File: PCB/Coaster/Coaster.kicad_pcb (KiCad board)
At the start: 2 copper layers, 202 x 100 mm, 88 parts, among them J1 Join, J2 Shelly, J3 USB-C, P1 TestPoint, P10 TestPoint, P11 TestPoint, P12 TestPoint, P13 TestPoint, P14 TestPoint, P15 TestPoint, P16 TestPoint, P17 TestPoint, P2 TestPoint, P3 TestPoint, P4 TestPoint, P5 TestPoint, P6 TestPoint, P7 TestPoint, P8 TestPoint, P9 TestPoint, T1 TestPoint, T10 TestPoint, T11 TestPoint, T12 TestPoint, T13 TestPoint, T14 TestPoint, T15 TestPoint, T16 TestPoint, T17 TestPoint, T2 TestPoint, T3 TestPoint, T4 TestPoint, T5 TestPoint, T6 TestPoint, T7 TestPoint, T8 TestPoint, T9 TestPoint, U1 ESP32-PICO-MINI-02, U2 LMR16006XDDCR, U3 QR

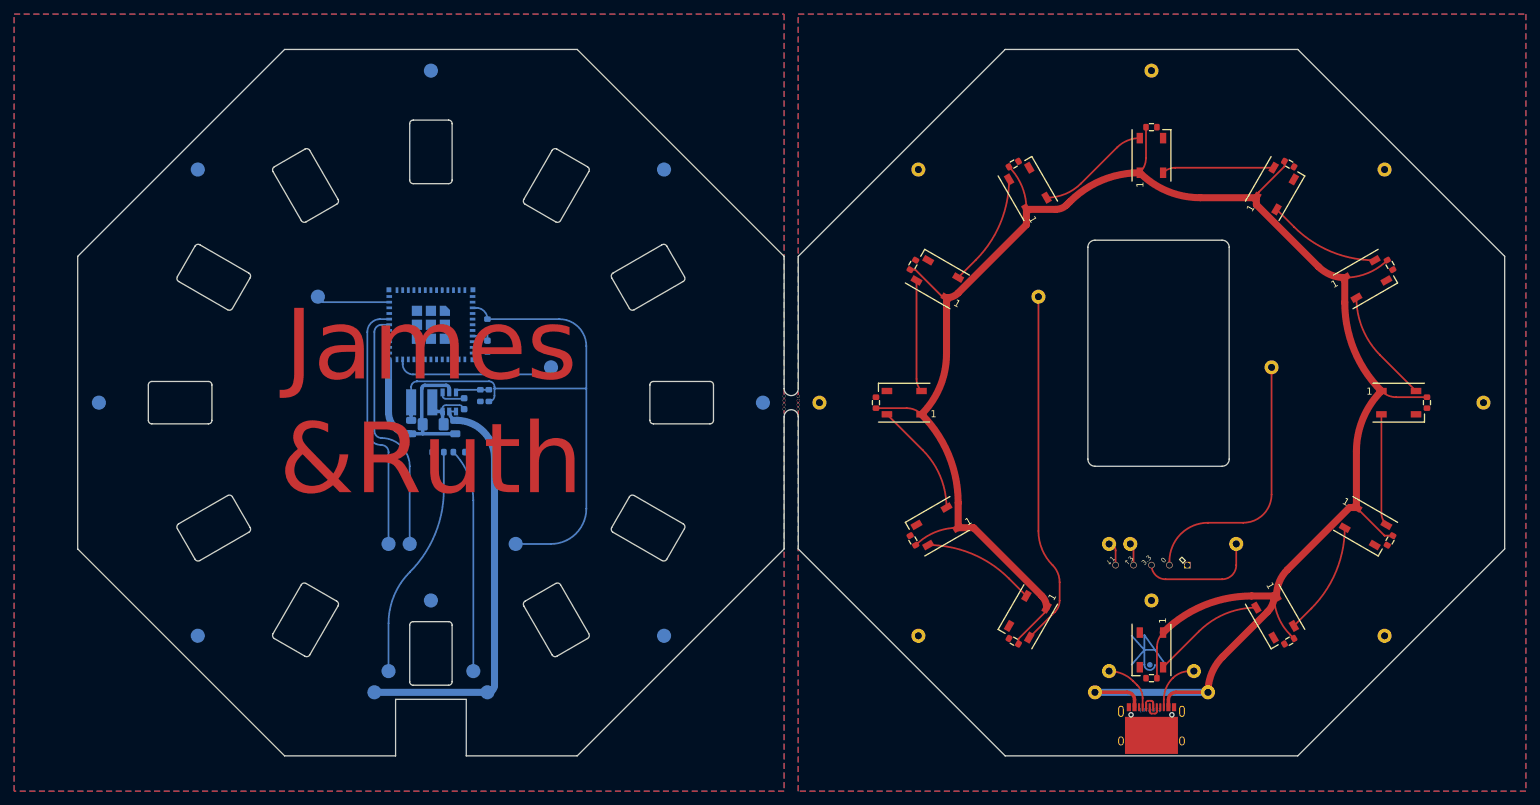
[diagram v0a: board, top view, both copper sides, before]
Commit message: Reworked for rubber feet
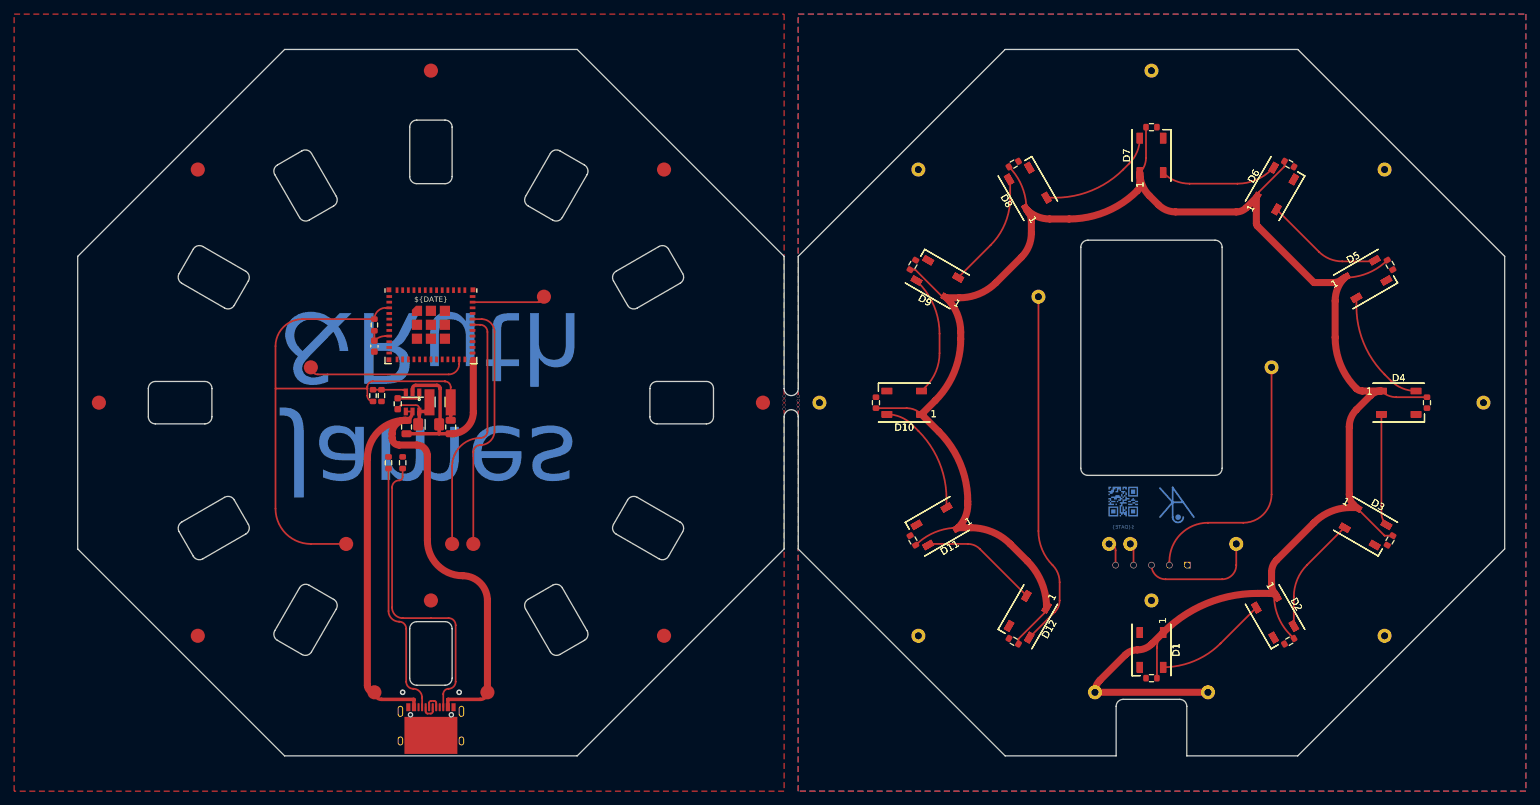
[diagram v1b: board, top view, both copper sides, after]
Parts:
- removed P3, P4: TestPoint, RevK:PAD
- removed T3, T4: TestPoint, RevK:PAD-LINK
- added D1: WS2818B, RevK:SMD5050, F.Cu at (201.0, 135.0)
- added D10: WS2818B, RevK:SMD5050, F.Cu at (166.0, 100.0)
- added D11: WS2818B, RevK:SMD5050, F.Cu at (170.7, 117.5)
- added D12: WS2818B, RevK:SMD5050, F.Cu at (183.5, 130.3)
- added D2: WS2818B, RevK:SMD5050, F.Cu at (218.5, 130.3)
- added D3: WS2818B, RevK:SMD5050, F.Cu at (231.3, 117.5)
- added D4: WS2818B, RevK:SMD5050, F.Cu at (236.0, 100.0)
- added D5: WS2818B, RevK:SMD5050, F.Cu at (231.3, 82.5)
- added D6: WS2818B, RevK:SMD5050, F.Cu at (218.5, 69.7)
- added D7: WS2818B, RevK:SMD5050, F.Cu at (201.0, 65.0)
- added D8: WS2818B, RevK:SMD5050, F.Cu at (183.5, 69.7)
- added D9: WS2818B, RevK:SMD5050, F.Cu at (170.7, 82.5)
- C13, C14, C15, C16, D14, L1, P1, P10, P11, P12, P13, P14, P15, P16, P17, P2, P5, P6, P7, P8, P9, R1, R5, R6, R7, R8, U1, U2: moved to F.Cu
- D1, D10, D11, D12, D2, D3, D4, D5, D6, D7, D8, D9: value WS2812B -> WS2818B; footprint LED_SMD:LED_WS2812B_PLCC4_5.0x5.0mm_P3.2mm -> RevK:SMD5050
- J2: moved to B.Cu
- moved J3 102.0 mm to (99.0, 145.6)
- moved P5 94.0 mm to (52.0, 100.0), turned to 0 degrees
- moved P6 94.0 mm to (146.0, 100.0), turned to 0 degrees
- moved P14 66.0 mm to (132.0, 133.0), turned to 0 degrees
- moved P15 66.0 mm to (66.0, 133.0), turned to 0 degrees
- moved P16 66.0 mm to (66.0, 67.0), turned to 0 degrees
- moved P17 66.0 mm to (132.0, 67.0), turned to 0 degrees
- moved P12 34.0 mm to (82.0, 95.0), turned to 0 degrees
- moved U3 33.3 mm to (197.0, 114.0), turned to 180 degrees
- moved P13 32.0 mm to (115.0, 85.0), turned to 0 degrees
- moved P11 24.0 mm to (87.0, 120.0), turned to 0 degrees
- moved Logo1 21.3 mm to (204.0, 114.1)
- moved R7 16.4 mm to (90.8, 99.0)
- moved C16 16.0 mm to (91.0, 92.0)
- moved P1 16.0 mm to (107.0, 141.0), turned to 0 degrees
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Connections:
- J3 pad A1: GND2 -> GND
- J3 pad A12: GND2 -> GND
- J3 pad A4: VCC -> VBUS
- J3 pad A9: VCC -> VBUS
- J3 pad B1: GND2 -> GND
- J3 pad B12: GND2 -> GND
- J3 pad B4: VCC -> VBUS
- J3 pad B9: VCC -> VBUS
- J3 pad S1: GND2 -> GND
- R5 pad 1: Net-(P3-Pad1) -> Net-(J3-PadB5)
- R6 pad 2: Net-(P4-Pad1) -> Net-(J3-PadA5)
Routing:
- net VBUS: track 58.8 -> 105.3 mm
- net Net-(J3-PadB5): track 7.09 -> 43.3 mm
- net Net-(P3-Pad1): track 33.0 -> 0.00 mm
- net Net-(P4-Pad1): track 31.7 -> 0.00 mm
- net Net-(J3-PadA5): track 7.90 -> 36.3 mm
- net VCC: track 319.7 -> 321.5 mm
- net Net-(D10-Pad2): track 15.8 -> 17.2 mm
- net Net-(D10-Pad4): track 16.1 -> 17.0 mm
- net Net-(D7-Pad4): track 16.1 -> 17.0 mm
- net Net-(D4-Pad4): track 16.1 -> 17.0 mm
- net Net-(D6-Pad4): track 15.8 -> 16.6 mm
- net Net-(D11-Pad4): track 16.1 -> 16.9 mm
- net Net-(D5-Pad4): track 16.1 -> 16.8 mm
- net Net-(D2-Pad4): track 16.1 -> 16.6 mm
- net GND: vias 0 -> 2
- removed copper zone on B.Cu, net GND
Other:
- outline, holes or cut-outs redrawn
- board text added: "LED GPIO 22"

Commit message: Tidy
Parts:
- moved Logo1 1.00 mm to (205.0, 114.1)
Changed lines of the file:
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@@
   )
   (footprint "RevK:AJK" (layer "B.Cu")
-    (at 204 114.1 180)
+    (at 205 114.1 180)
     (property "Note" "Non part, PCB printed")
     (property "Sheetfile" "Coaster.kicad_sch")

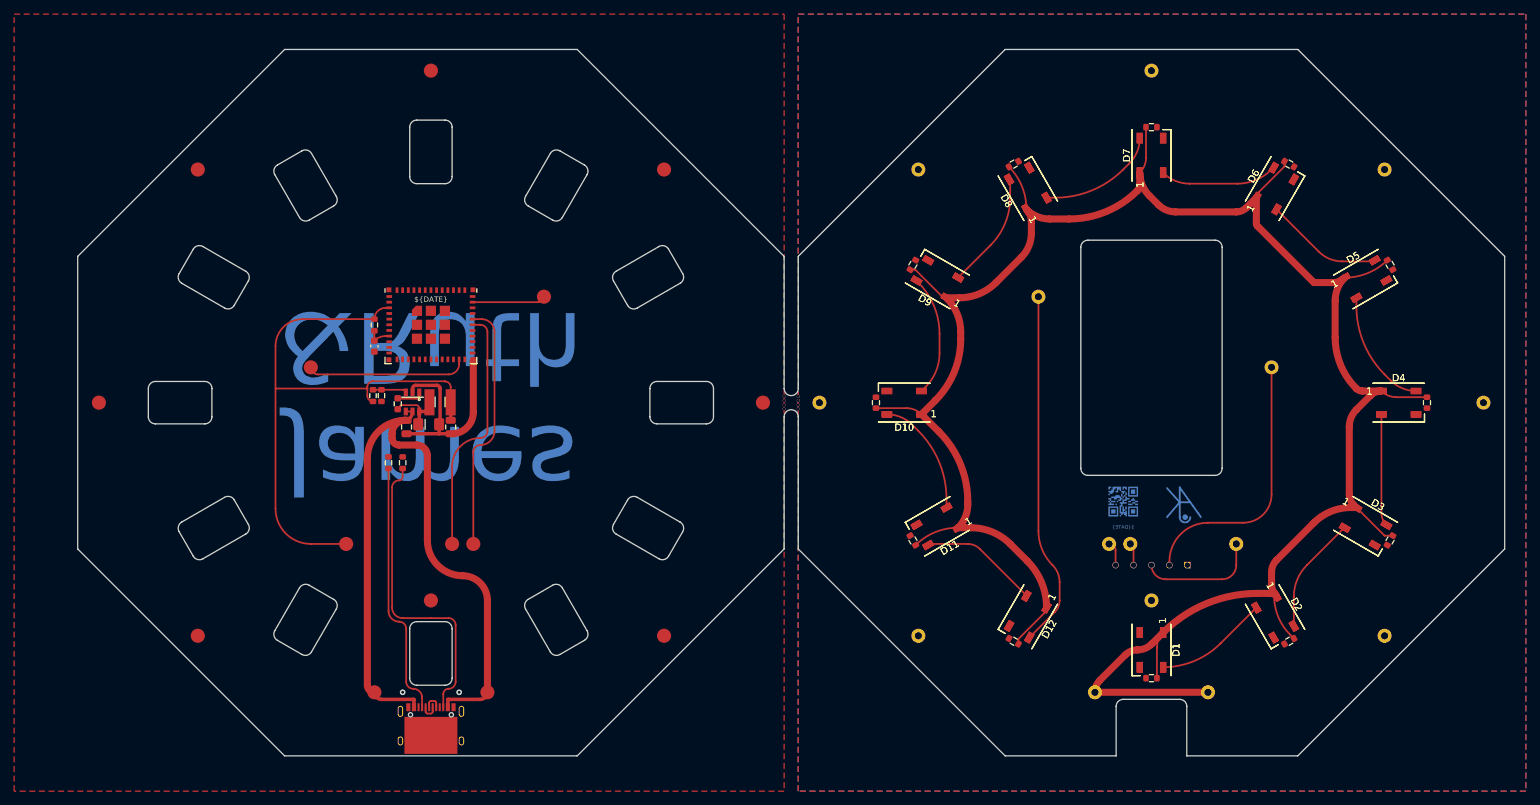
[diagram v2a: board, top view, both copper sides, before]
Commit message: 12 sided
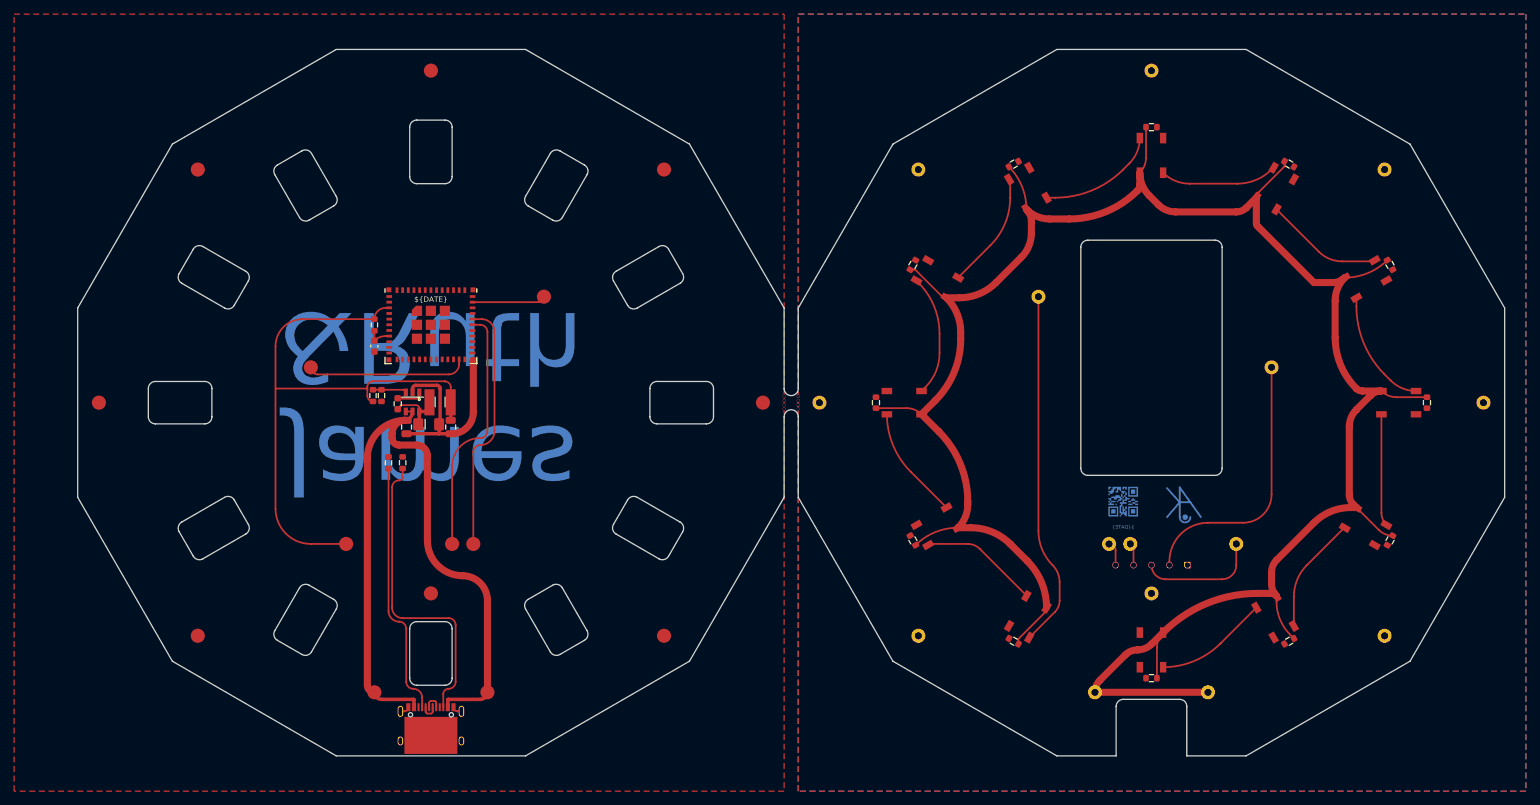
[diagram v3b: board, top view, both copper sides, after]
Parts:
- removed the D1 at (201.0, 135.0) (x2)
- removed the D10 at (166.0, 100.0) (x2)
- removed the D11 at (170.7, 117.5) (x2)
- removed the D12 at (183.5, 130.3) (x2)
- removed the D2 at (218.5, 130.3) (x2)
- removed the D3 at (231.3, 117.5) (x2)
- removed the D4 at (236.0, 100.0) (x2)
- removed the D5 at (231.3, 82.5) (x2)
- removed the D6 at (218.5, 69.7) (x2)
- removed the D7 at (201.0, 65.0) (x2)
- removed the D8 at (183.5, 69.7) (x2)
- removed the D9 at (170.7, 82.5) (x2)
- added D1: WS2818B, RevK:SMD5050, F.Cu at (201.0, 135.0)
- added D10: WS2818B, RevK:SMD5050, F.Cu at (166.0, 100.0)
- added D11: WS2818B, RevK:SMD5050, F.Cu at (170.7, 117.5)
- added D12: WS2818B, RevK:SMD5050, F.Cu at (183.5, 130.3)
- added D2: WS2818B, RevK:SMD5050, F.Cu at (218.5, 130.3)
- added D3: WS2818B, RevK:SMD5050, F.Cu at (231.3, 117.5)
- added D4: WS2818B, RevK:SMD5050, F.Cu at (236.0, 100.0)
- added D5: WS2818B, RevK:SMD5050, F.Cu at (231.3, 82.5)
- added D6: WS2818B, RevK:SMD5050, F.Cu at (218.5, 69.7)
- added D7: WS2818B, RevK:SMD5050, F.Cu at (201.0, 65.0)
- added D8: WS2818B, RevK:SMD5050, F.Cu at (183.5, 69.7)
- added D9: WS2818B, RevK:SMD5050, F.Cu at (170.7, 82.5)
- moved P8 1.00 mm to (99.0, 127.0)
- moved T8 1.00 mm to (201.0, 127.0)
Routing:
- net GND: track 12.0 -> 14.9 mm, vias 2 -> 0
- net Net-(D10-Pad4): track 17.0 -> 16.1 mm
- net Net-(D11-Pad4): track 16.9 -> 16.4 mm
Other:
- outline, holes or cut-outs redrawn

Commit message: Much tidying
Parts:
- removed P13, P14, P15, P16, P17: TestPoint, RevK:PAD
- removed R6: 5K1, RevK:R_0603
- removed R7: 100k 1%, RevK:R_0603
- removed R8: 30k 1%, RevK:R_0603
- removed T13, T14, T15, T16, T17: TestPoint, RevK:PAD-LINK
- added C17: 10nF, RevK:C_0603, F.Cu at (229.3, 80.9)
- added C18: 10nF, RevK:C_0603, F.Cu at (233.3, 89.1)
- added C19: 10nF, RevK:C_0603, F.Cu at (234.9, 98.1)
- added C20: 10nF, RevK:C_0603, F.Cu at (234.2, 107.2)
- added C21: 10nF, RevK:C_0603, F.Cu at (231.2, 115.8)
- added C22: 10nF, RevK:C_0603, F.Cu at (226.1, 123.4)
- added C23: 10nF, RevK:C_0603, F.Cu at (219.1, 129.3)
- added C24: 10nF, RevK:C_0603, F.Cu at (210.9, 133.3)
- added C25: 10nF, RevK:C_0603, F.Cu at (198.1, 134.9)
- added C26: 10nF, RevK:C_0603, F.Cu at (189.1, 133.3)
- added C27: 10nF, RevK:C_0603, F.Cu at (180.9, 129.3)
- added C28: 10nF, RevK:C_0603, F.Cu at (173.9, 123.4)
- added C29: 10nF, RevK:C_0603, F.Cu at (168.8, 115.8)
- added C30: 10nF, RevK:C_0603, F.Cu at (165.8, 107.2)
- added C31: 10nF, RevK:C_0603, F.Cu at (165.1, 98.1)
- added C32: 10nF, RevK:C_0603, F.Cu at (166.7, 89.1)
- added C33: 10nF, RevK:C_0603, F.Cu at (170.7, 80.9)
- added C34: 10nF, RevK:C_0603, F.Cu at (176.6, 74.0)
- added C35: 10nF, RevK:C_0603, F.Cu at (184.2, 68.8)
- added C36: 10nF, RevK:C_0603, F.Cu at (192.8, 65.8)
- added C37: 10nF, RevK:C_0603, F.Cu at (201.9, 65.0)
- added C38: 10nF, RevK:C_0603, F.Cu at (210.9, 66.7)
- added C39: 10nF, RevK:C_0603, F.Cu at (219.1, 70.7)
- added C40: 10nF, RevK:C_0603, F.Cu at (226.1, 76.6)
- added C41: 10nF, RevK:C_0603, F.Cu at (231.2, 84.2)
- added C42: 10nF, RevK:C_0603, F.Cu at (234.2, 92.8)
- added C43: 10nF, RevK:C_0603, F.Cu at (234.9, 101.9)
- added C44: 10nF, RevK:C_0603, F.Cu at (233.3, 110.9)
- added C45: 10nF, RevK:C_0603, F.Cu at (229.3, 119.1)
- added C46: 10nF, RevK:C_0603, F.Cu at (223.4, 126.0)
- added C47: 10nF, RevK:C_0603, F.Cu at (215.8, 131.2)
- added C48: 10nF, RevK:C_0603, F.Cu at (207.2, 134.2)
- added C49: 10nF, Capacitor_SMD:C_0603_1608Metric, F.Cu at (92.0, 91.0)
- added C50: 100nF, RevK:C_0603_, F.Cu at (94.3, 100.2)
- added C51: 2.2uF, RevK:C_0805_, F.Cu at (95.5, 103.5)
- added C52: 10uF, RevK:C_0805_, F.Cu at (101.8, 103.5)
- added D13: WS2818B, RevK:SMD2020, F.Cu at (200.0, 65.0)
- added D15: WS2818B, RevK:SMD2020, F.Cu at (217.5, 69.7)
- added D16: WS2818B, RevK:SMD2020, F.Cu at (224.8, 75.2)
- added D17: WS2818B, RevK:SMD2020, F.Cu at (230.3, 82.5)
- added D18: WS2818B, RevK:SMD2020, F.Cu at (233.8, 90.9)
- added D19: WS2818B, RevK:SMD2020, F.Cu at (235.0, 100.0)
- added D20: WS2818B, RevK:SMD2020, F.Cu at (233.8, 109.1)
- added D21: WS2818B, RevK:SMD2020, F.Cu at (230.3, 117.5)
- added D22: WS2818B, RevK:SMD2020, F.Cu at (224.8, 124.8)
- added D23: WS2818B, RevK:SMD2020, F.Cu at (217.5, 130.3)
- added D24: WS2818B, RevK:SMD2020, F.Cu at (209.1, 133.8)
- added D25: Schottky, RevK:D_1206_, F.Cu at (98.7, 103.1)
- added H13: MountingHole, RevK:LEDHOLE, F.Cu at (100.0, 65.0)
- added H14: MountingHole, RevK:LEDHOLE, F.Cu at (109.1, 66.2)
- added H15: MountingHole, RevK:LEDHOLE, F.Cu at (117.5, 69.7)
- added H16: MountingHole, RevK:LEDHOLE, F.Cu at (124.8, 75.2)
- added H17: MountingHole, RevK:LEDHOLE, F.Cu at (130.3, 82.5)
- added H18: MountingHole, RevK:LEDHOLE, F.Cu at (133.8, 90.9)
- added H19: MountingHole, RevK:LEDHOLE, F.Cu at (135.0, 100.0)
- added H20: MountingHole, RevK:LEDHOLE, F.Cu at (133.8, 109.1)
- added H21: MountingHole, RevK:LEDHOLE, F.Cu at (130.3, 117.5)
- added H22: MountingHole, RevK:LEDHOLE, F.Cu at (124.8, 124.8)
- added H23: MountingHole, RevK:LEDHOLE, F.Cu at (117.5, 130.3)
- added H24: MountingHole, RevK:LEDHOLE, F.Cu at (109.1, 133.8)
- added P3: TestPoint, RevK:PAD, F.Cu at (113.0, 88.0)
- added P4: TestPoint, RevK:PAD, F.Cu at (113.0, 91.0)
- added R2: 5K1, RevK:R_0603, F.Cu at (96.6, 108.0)
- added R3: 5K1, RevK:R_0603, F.Cu at (98.0, 108.0)
- added R4: 100k 1%, RevK:R_0603, F.Cu at (93.0, 98.0)
- added T3: TestPoint, RevK:PAD-LINK, F.Cu at (187.0, 88.0)
- added T4: TestPoint, RevK:PAD-LINK, F.Cu at (187.0, 91.0)
- C13: value 100nF -> 10nF; footprint RevK:C_0603_ -> RevK:C_0603
- C14: value 2.2uF -> 10nF; footprint RevK:C_0805_ -> RevK:C_0603
- C15: value 10uF -> 10nF; footprint RevK:C_0805_ -> RevK:C_0603
- C16: footprint Capacitor_SMD:C_0603_1608Metric -> RevK:C_0603
- D1, D10, D11, D12, D2, D3, D4, D5, D6, D7, D8, D9: footprint RevK:SMD5050 -> RevK:SMD2020
- D14: value Schottky -> WS2818B; footprint RevK:D_1206_ -> RevK:SMD2020
- J1: value Join -> USB-C; footprint RevK:PCB-Join -> RevK:USC16-TR
- J3: value USB-C -> Join; footprint RevK:USC16-TR -> RevK:PCB-Join
- R5: value 5K1 -> 30k 1%
- moved C16 133.6 mm to (223.4, 74.0), turned to 45 degrees
- moved C15 119.2 mm to (215.8, 68.8), turned to 60 degrees
- moved C14 117.9 mm to (207.2, 65.8), turned to 75 degrees
- moved D14 116.4 mm to (209.1, 66.2), turned to 75 degrees
- moved C13 109.6 mm to (198.1, 65.0), turned to 90 degrees
- moved P7 86.3 mm to (114.0, 138.0)
- moved T7 86.3 mm to (186.0, 138.0)
- moved C5 74.8 mm to (170.7, 119.1), turned to -150 degrees
- moved P8 74.0 mm to (100.0, 53.0)
- moved T8 74.0 mm to (200.0, 53.0)
- moved D5 70.9 mm to (169.7, 117.5), turned to -150 degrees
- moved C6 69.9 mm to (166.7, 110.9), turned to -165 degrees
- moved H5 69.1 mm to (69.7, 117.5), turned to 120 degrees
- moved C4 68.5 mm to (176.6, 126.0), turned to -135 degrees
- moved J3 68.4 mm to (150.0, 100.0)
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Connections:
- C16 pad 1: GND -> VCC
- C16 pad 2: Net-(C16-Pad2) -> GND2
- D1 pad 2: unconnected-(D1-Pad2) -> Net-(D1-Pad2)
- D1 pad 4: Net-(D1-Pad4) -> LED
- D11 pad 2: Net-(D10-Pad4) -> Net-(D11-Pad2)
- D11 pad 4: Net-(D11-Pad4) -> Net-(D10-Pad2)
- D12 pad 2: Net-(D11-Pad4) -> Net-(D12-Pad2)
- D12 pad 4: LED -> Net-(D11-Pad2)
- D2 pad 2: Net-(D1-Pad4) -> Net-(D2-Pad2)
- D2 pad 4: Net-(D2-Pad4) -> Net-(D1-Pad2)
- D3 pad 2: Net-(D2-Pad4) -> Net-(D3-Pad2)
- D3 pad 4: Net-(D3-Pad4) -> Net-(D2-Pad2)
- D4 pad 2: Net-(D3-Pad4) -> Net-(D4-Pad2)
- D4 pad 4: Net-(D4-Pad4) -> Net-(D3-Pad2)
- D5 pad 2: Net-(D4-Pad4) -> Net-(D5-Pad2)
- D5 pad 4: Net-(D5-Pad4) -> Net-(D4-Pad2)
- D6 pad 2: Net-(D5-Pad4) -> Net-(D6-Pad2)
- D6 pad 4: Net-(D6-Pad4) -> Net-(D5-Pad2)
- D7 pad 2: Net-(D6-Pad4) -> Net-(D7-Pad2)
- D7 pad 4: Net-(D7-Pad4) -> Net-(D6-Pad2)
- D8 pad 2: Net-(D7-Pad4) -> Net-(D8-Pad2)
- D8 pad 4: Net-(D8-Pad4) -> Net-(D7-Pad2)
- D9 pad 2: Net-(D8-Pad4) -> Net-(D10-Pad4)
- D9 pad 4: Net-(D10-Pad2) -> Net-(D8-Pad2)
- P10 pad 1: Net-(P10-Pad1) -> GND
- P11 pad 1: +3V3 -> GND
- P12 pad 1: Net-(P12-Pad1) -> GND
- P5 pad 1: GND -> +3V3
- P6 pad 1: GND -> Net-(P6-Pad1)
- P7 pad 1: GND -> Net-(P7-Pad1)
- P9 pad 1: Net-(P9-Pad1) -> GND
- R1 pad 2: Net-(C16-Pad2) -> Net-(C49-Pad2)
- R5 pad 1: Net-(J3-PadB5) -> GND
- R5 pad 2: GND -> Net-(R4-Pad2)
- T10 pad 1: I -> GND2
- T11 pad 1: +3.3VA -> GND2
- T12 pad 1: GPIO0 -> GND2
- T5 pad 1: GND2 -> +3.3VA
- T6 pad 1: GND2 -> GPIO0
- T7 pad 1: GND2 -> LED
- T9 pad 1: O -> GND2
- U1 pad 23: Net-(P12-Pad1) -> Net-(P6-Pad1)
- U1 pad 30: Net-(P10-Pad1) -> Net-(P4-Pad1)
- U1 pad 31: Net-(P9-Pad1) -> Net-(P3-Pad1)
- U1 pad 34: Net-(P13-Pad1) -> Net-(P7-Pad1)
- U1 pad 8: Net-(C16-Pad2) -> Net-(C49-Pad2)
- U2 pad 3: Net-(R7-Pad2) -> Net-(R4-Pad2)
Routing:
- net VCC: track 321.3 -> 22.4 mm
- net Net-(P7-Pad1): track 0.00 -> 66.4 mm
- net Net-(J3-PadB5): track 43.3 -> 0.00 mm
- net Net-(J3-PadA5): track 36.3 -> 0.00 mm
- net Net-(J1-PadB5): track 0.00 -> 36.3 mm
- net Net-(P9-Pad1): track 35.7 -> 0.00 mm
- net Net-(P10-Pad1): track 35.3 -> 0.00 mm
- net LED: track 50.7 -> 15.6 mm
- net Net-(J1-PadA5): track 0.00 -> 34.2 mm
- net +3V3: track 84.9 -> 61.4 mm
- net Net-(P12-Pad1): track 23.0 -> 0.00 mm
- net GPIO0: track 38.0 -> 17.9 mm
- net Net-(D7-Pad4): track 17.0 -> 0.00 mm
- net Net-(D4-Pad4): track 17.0 -> 0.00 mm
- net Net-(D2-Pad4): track 16.5 -> 0.00 mm
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- added copper zone on F.Cu, net VCC
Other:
- board size 202 x 100 mm -> 198 x 98 mm
